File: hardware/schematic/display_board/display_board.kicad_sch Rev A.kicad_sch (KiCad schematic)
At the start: 7 parts, among them J1 RS232 to Display, J2 Flow Meter, J3 Depth Sensor, J4 Picoblade to GPS

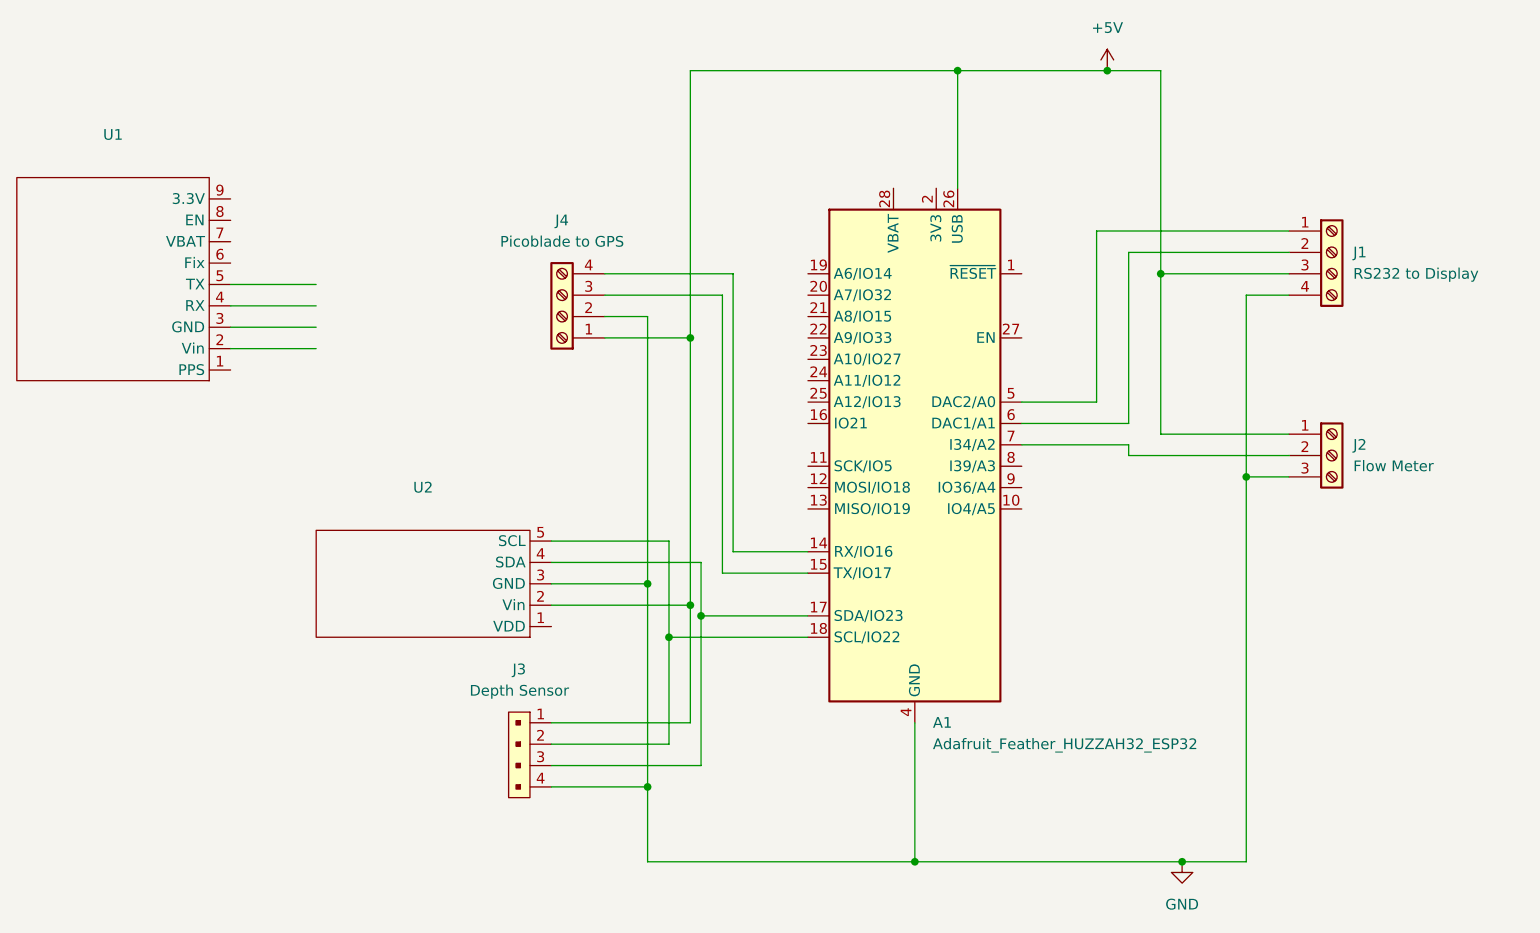
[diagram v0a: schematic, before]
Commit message: First commit of PCB files for NAV and DISPLAY boards
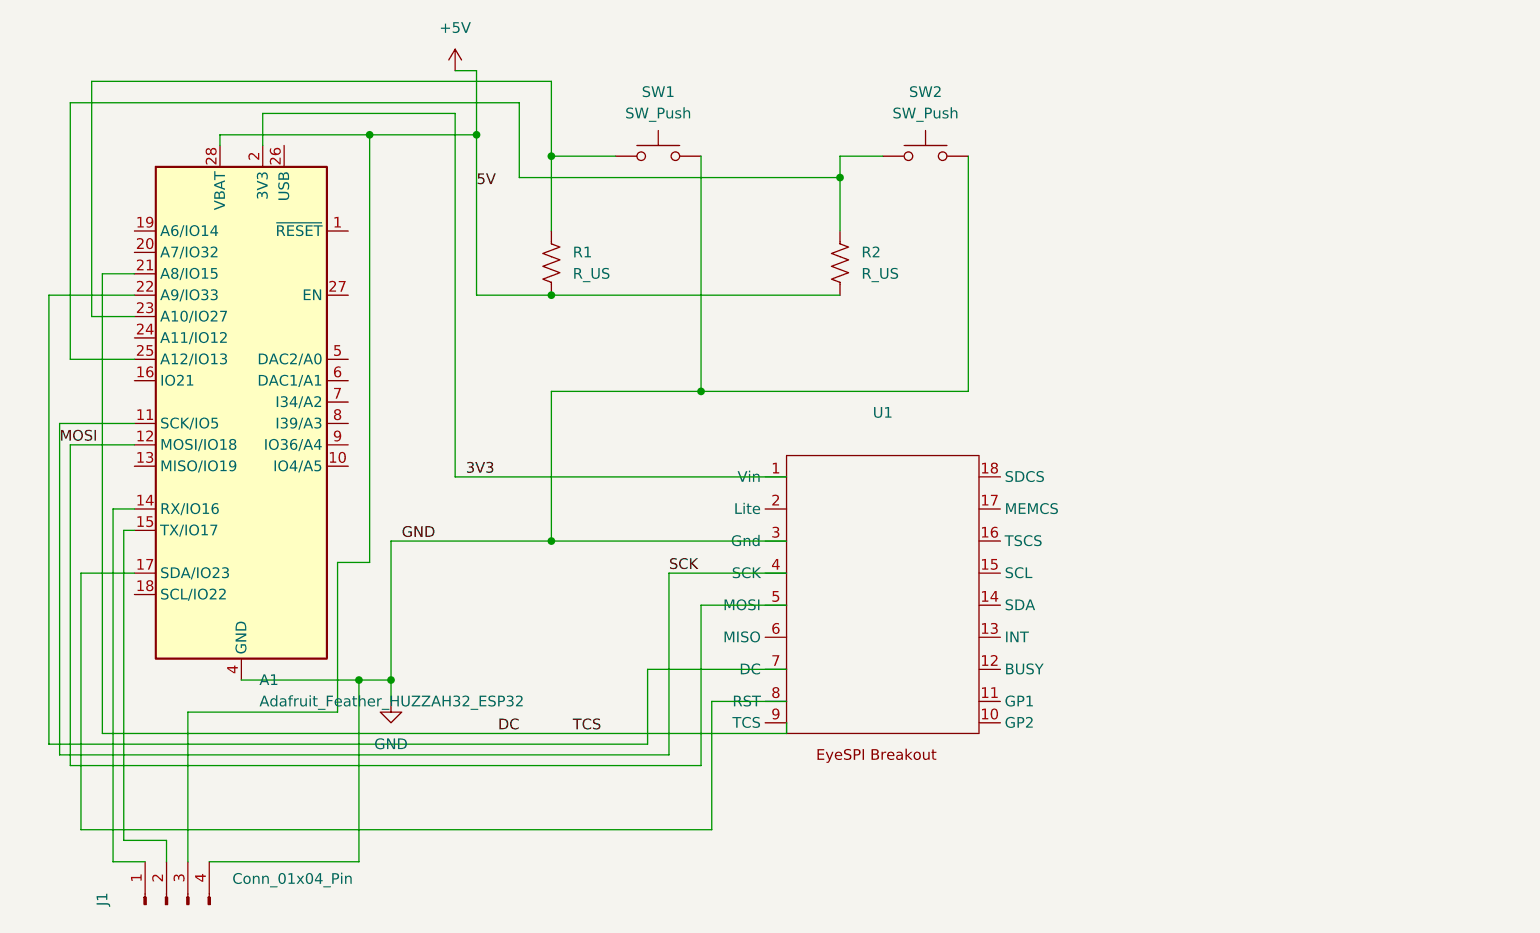
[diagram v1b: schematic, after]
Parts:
- removed J1: RS232 to Display, Connector_Molex:Molex_PicoBlade_53047-0410_1x04_P1.25mm_Vertical, symbol Connector:Screw_Terminal_01x04
- removed J2: Flow Meter, Connector_Molex:Molex_PicoBlade_53047-0310_1x03_P1.25mm_Vertical, symbol Connector:Screw_Terminal_01x03
- removed J3: Depth Sensor, Connector_Molex:Molex_PicoBlade_53047-0410_1x04_P1.25mm_Vertical, symbol dk_Rectangular-Connectors-Headers-Male-Pins:B4B-XH-A_LF__SN_
- removed J4: Picoblade to GPS, Connector_Molex:Molex_PicoBlade_53047-0410_1x04_P1.25mm_Vertical, symbol Connector:Screw_Terminal_01x04
- removed U1: ~, DPVNav Footprint Library:Adafruit Ultimate GPS, symbol MCU_Module:Adafruit_Ultimate_GPS
- removed U2: ~, DPVNav Footprint Library:Pololu Altimu-10 v5, symbol MCU_Module:Pololu_Altimu-10_v5
- added J1: Conn_01x04_Pin, Connector_Molex:Molex_PicoBlade_53047-0410_1x04_P1.25mm_Vertical, symbol Connector:Conn_01x04_Pin
- added R1, R2: R_US, Resistor_THT:R_Axial_DIN0207_L6.3mm_D2.5mm_P7.62mm_Horizontal, symbol Device:R_US
- added SW1, SW2: SW_Push, Connector_Molex:Molex_PicoBlade_53047-0210_1x02_P1.25mm_Vertical, symbol Switch:SW_Push
- added U1: ~, DPV_Nav_Library:EyeSPI_Breakout, symbol New_Library:EyeSpi_Breakout
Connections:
- net +5V: now also A1.28 (VBAT), J1.3 (Pin_3), R1.2, R2.2; no longer A1.26 (USB)
- net GND: now also J1.4 (Pin_4), SW1.2, SW2.2, U1.3 (Gnd)
- net at A1.15 (TX/IO17): now also J1.2 (Pin_2)
- net at A1.14 (RX/IO16): now also J1.1 (Pin_1)
- net MOSI: now reaches A1.11 (SCK/IO5)
- net MOSI: now also U1.4 (SCK)
- net at A1.12 (MOSI/IO18): now also U1.5 (MOSI)
- net at A1.17 (SDA/IO23): now also U1.8 (RST)
- net 3V3: now reaches A1.2 (3V3)
- net 3V3: now also U1.1 (Vin)
- net DC: now reaches A1.21 (A8/IO15)
- net DC: now also U1.9 (TCS)
- net at A1.22 (A9/IO33): now also U1.7 (DC)
- net at A1.23 (A10/IO27): now also R1.1, SW1.1
- net at A1.25 (A12/IO13): now also R2.1, SW2.1
